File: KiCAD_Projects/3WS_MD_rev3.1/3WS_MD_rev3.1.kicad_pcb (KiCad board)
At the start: 2 copper layers, 76 x 93 mm, 139 parts, among them P1 CONN_01X01, P10 CONN_01X04, P11 TST, P12 TST, P13 CONN_01X06, P14 CONN_01X02, P15 CONN_01X02, P16 CONN_01X04, P17 CONN_01X04, P18 CONN_01X04, P19 CONN_01X04, P2 CONN_01X01, P20 CONN_01X03, P3 CONN_01X04, P4 CONN_02X06, P5 TST, P6 CONN_01X04, P7 CONN_01X02, P8 CONN_01X04, P9 TST, Q1 MOSFET_N, Q2 MOSFET_N, Q3 MOSFET_N, Q4 MOSFET_N, Q5 MOSFET_N, Q6 MOSFET_N, Q7 MOSFET_N, Q8 MOSFET_N, SW1 SW_PUSH, SW2 SW_PUSH, SW3 SW_PUSH, U1 STM32F103_48, U10 NCP1117ST33T3G, U2 SI8234, U3 SI8234, U4 LM7812, U5 SI8234, U6 SI8234, U7 NCP1117ST33T3G, U8 MAX3051, U9 SW_ROTARY_16, X2 CRYSTAL

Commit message: no message
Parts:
- removed C22: 470u, Capacitors_ThroughHole:C_Radial_D12.5_L25_P5
- C27: moved to F.Cu
- P1: value CONN_01X01 -> CONN_01X02; footprint Connect:1pin -> RP_KiCAD_Connector:DEANS_T_M
- P2: value CONN_01X01 -> CONN_01X02; footprint Connect:1pin -> RP_KiCAD_Connector:DEANS_T_F
- SW1, SW2, SW3: footprint RP_KiCAD_Libs:RP_SMD_Button -> Buttons_Switches_SMD:RP_SMD_Button
- moved C25 16.4 mm to (9.00, 39.0)
- moved C30 16.4 mm to (9.00, 41.5)
- moved P2 15.7 mm to (7.00, 33.5), turned to 270 degrees
- moved D12 12.5 mm to (17.5, 38.5)
- moved R20 11.9 mm to (15.0, 38.5)
- moved U4 8.14 mm to (15.5, 41.0), turned to 0 degrees
- moved C21 6.71 mm to (9.00, 44.0)
- moved C28 5.50 mm to (17.5, 43.0), turned to 270 degrees
- moved D15 5.39 mm to (17.5, 35.5)
- moved P1 5.22 mm to (7.00, 25.0), turned to 270 degrees
- moved P12 4.00 mm to (72.0, 40.5)
- moved P6 3.00 mm to (12.5, 14.5)
- moved C27 2.24 mm to (14.5, 43.0), turned to 270 degrees
- moved FB3 1.00 mm to (21.5, 20.5)
- moved FB7 1.00 mm to (47.5, 20.5)
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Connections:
- P1 pad 1: GNDPWR -> +BATT
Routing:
- net +BATT: track 40.1 -> 264.5 mm, vias 0 -> 156
- net /OUT_BN: track 16.9 -> 95.5 mm, vias 1 -> 36
- net /OUT_A: track 16.9 -> 91.4 mm, vias 1 -> 39
- net /OUT_AN: track 16.8 -> 86.8 mm, vias 1 -> 36
- net /OUT_B: track 16.9 -> 84.5 mm, vias 1 -> 39
- net GNDPWR: track 130.1 -> 172.4 mm, vias 11 -> 31
- net /GD_12V: track 110.1 -> 93.0 mm
- net GND: track 363.0 -> 370.5 mm, vias 49 -> 51
- net Net-(FB7-Pad2): track 3.05 -> 4.88 mm
- net Net-(D12-Pad2): track 1.50 -> 2.50 mm
- net /ENC_Ab: track 36.8 -> 37.8 mm
- net /ENC_Aa: track 42.9 -> 43.8 mm
- net Net-(C27-Pad1): track 8.87 -> 8.07 mm, vias 0 -> 1
- net (no net): vias 8 -> 11
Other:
- board text removed: "BATT+"
- board text removed: "GND"

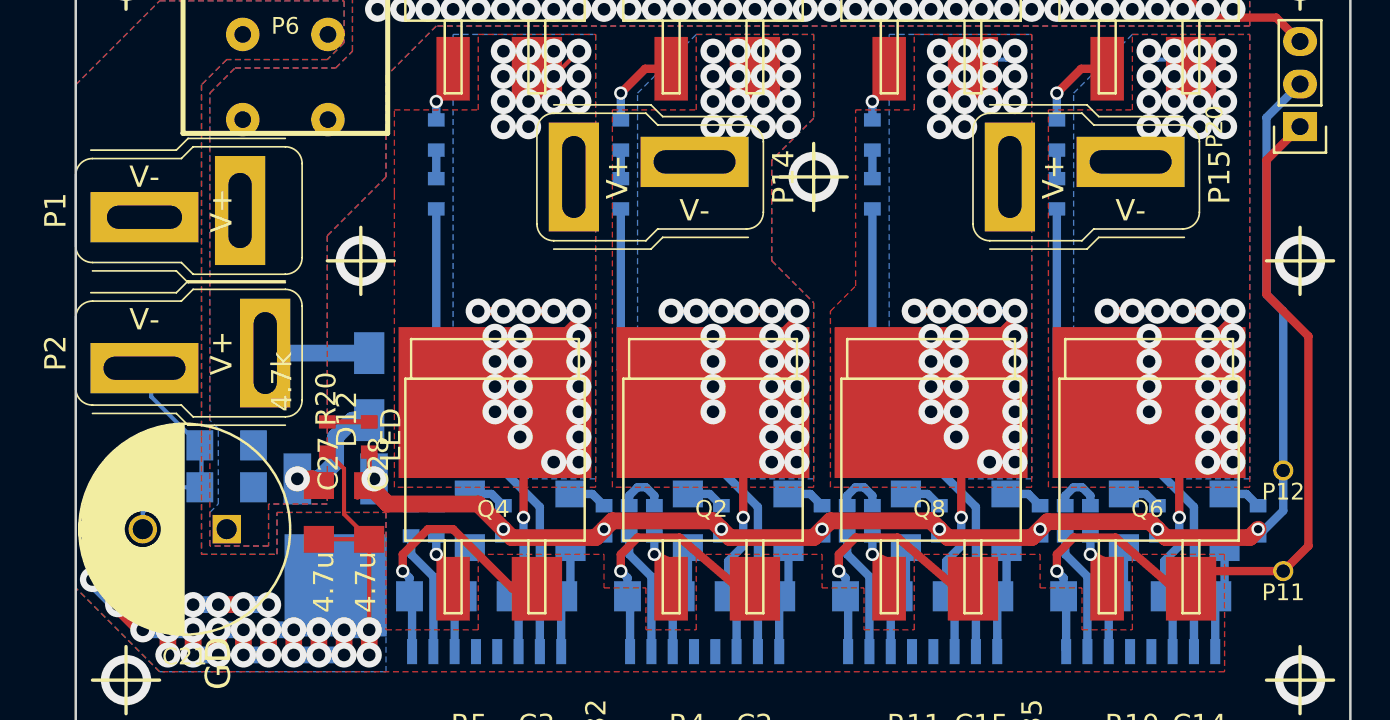
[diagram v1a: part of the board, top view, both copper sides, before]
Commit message: SPIアイソレータの追加
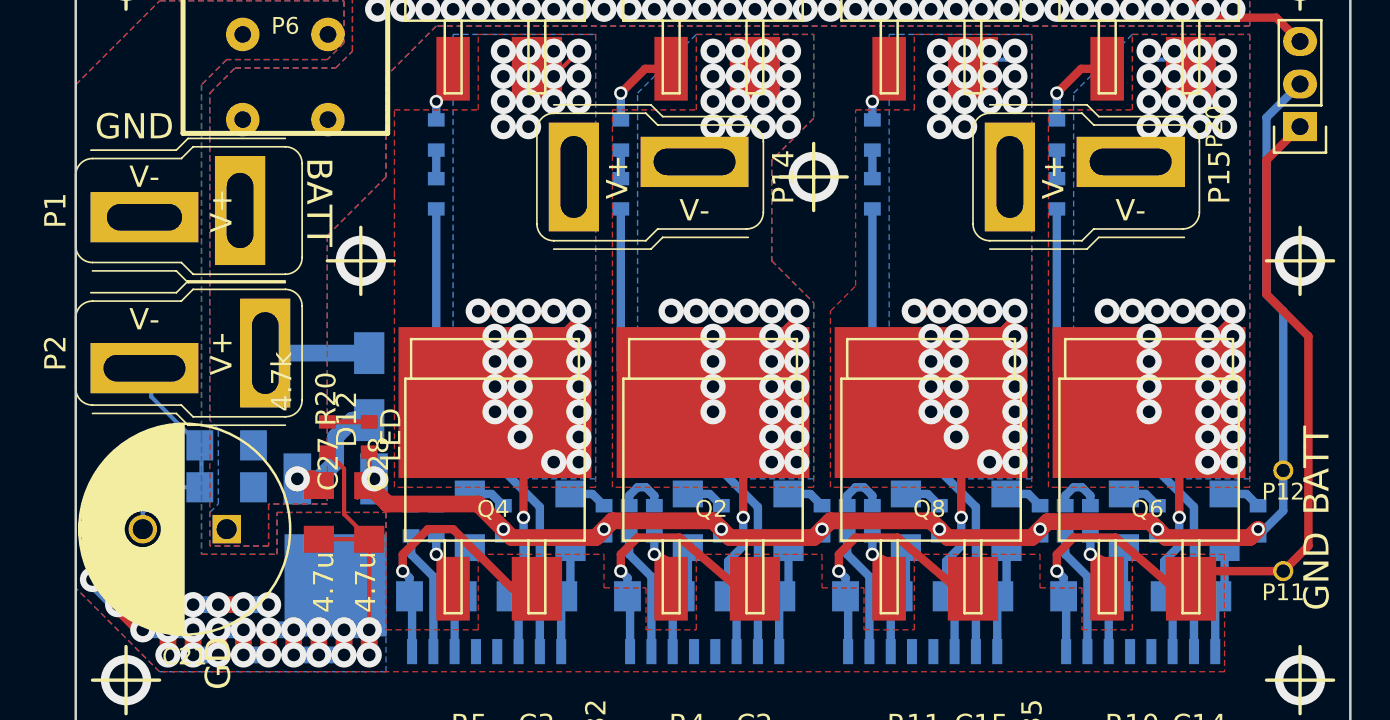
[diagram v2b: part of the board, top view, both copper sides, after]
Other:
- board text added: "BATT"
- board text added: "GND"

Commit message: 3Dデータ組み合わてテスト
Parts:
- added REF**: TSSOP-8_3x3mm_Pitch0.65mm, Housings_SSOP:TSSOP-8_3x3mm_Pitch0.65mm, F.Cu at (0.00, 0.00)
- R10, R11, R4, R5: value 10k -> 10-100k
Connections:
- P4 pad 2: Net-(C23-Pad1) -> +12V
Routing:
- net Net-(C23-Pad1): track 36.7 -> 16.2 mm
- net +12V: track 26.8 -> 45.5 mm, vias 1 -> 2
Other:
- board text added: "12V"

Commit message: no message
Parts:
- removed REF**: TSSOP-8_3x3mm_Pitch0.65mm, Housings_SSOP:TSSOP-8_3x3mm_Pitch0.65mm
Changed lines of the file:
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@@
     (tracks 1851)
     (zones 0)
-    (modules 139)
+    (modules 138)
     (nets 111)
   )
@@
     )
   )
-  (module Housings_SSOP:TSSOP-8_3x3mm_Pitch0.65mm (layer F.Cu)
-    (at 0 0)
-    (descr "TSSOP8: plastic thin shrink small outline package; 8 leads; body width 3 mm; (see NXP SSOP-TSSOP-VSO-REFLOW.pdf and sot505-1_po.pdf)")
-    (tags "SSOP 0.65")
-    (attr smd)
-    (fp_text reference REF** (at 0 -2.55) (layer F.SilkS)
-      (effects (font (size 1 1) (thickness 0.15)))
-    )
-    (fp_text value TSSOP-8_3x3mm_Pitch0.65mm (at 0 2.55) (layer F.Fab)
-      (effects (font (size 1 1) (thickness 0.15)))
-    )
-    (fp_line (start -2.95 -1.8) (end -2.95 1.8) (layer F.CrtYd) (width 0.05))
-    (fp_line (start 2.95 -1.8) (end 2.95 1.8) (layer F.CrtYd) (width 0.05))
-    (fp_line (start -2.95 -1.8) (end 2.95 -1.8) (layer F.CrtYd) (width 0.05))
-    (fp_line (start -2.95 1.8) (end 2.95 1.8) (layer F.CrtYd) (width 0.05))
-    (fp_line (start -1.625 -1.625) (end -1.625 -1.4) (layer F.SilkS) (width 0.15))
-    (fp_line (start 1.625 -1.625) (end 1.625 -1.4) (layer F.SilkS) (width 0.15))
-    (fp_line (start 1.625 1.625) (end 1.625 1.4) (layer F.SilkS) (width 0.15))
-    (fp_line (start -1.625 1.625) (end -1.625 1.4) (layer F.SilkS) (width 0.15))
-    (fp_line (start -1.625 -1.625) (end 1.625 -1.625) (layer F.SilkS) (width 0.15))
-    (fp_line (start -1.625 1.625) (end 1.625 1.625) (layer F.SilkS) (width 0.15))
-    (fp_line (start -1.625 -1.4) (end -2.7 -1.4) (layer F.SilkS) (width 0.15))
-    (pad 1 smd rect (at -2.15 -0.975) (size 1.1 0.4) (layers F.Cu F.Paste F.Mask))
-    (pad 2 smd rect (at -2.15 -0.325) (size 1.1 0.4) (layers F.Cu F.Paste F.Mask))
-    (pad 3 smd rect (at -2.15 0.325) (size 1.1 0.4) (layers F.Cu F.Paste F.Mask))
-    (pad 4 smd rect (at -2.15 0.975) (size 1.1 0.4) (layers F.Cu F.Paste F.Mask))
-    (pad 5 smd rect (at 2.15 0.975) (size 1.1 0.4) (layers F.Cu F.Paste F.Mask))
-    (pad 6 smd rect (at 2.15 0.325) (size 1.1 0.4) (layers F.Cu F.Paste F.Mask))
-    (pad 7 smd rect (at 2.15 -0.325) (size 1.1 0.4) (layers F.Cu F.Paste F.Mask))
-    (pad 8 smd rect (at 2.15 -0.975) (size 1.1 0.4) (layers F.Cu F.Paste F.Mask))
-    (model user/3WS_MD_rev3.1_Extension.wrl
-      (at (xyz 0 0 0.7))
-      (scale (xyz 1 1 1))
-      (rotate (xyz 0 0 0))
-    )
-  )
